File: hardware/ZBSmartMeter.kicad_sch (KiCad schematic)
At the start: 37 parts, among them J1 RJ12, J2 Conn_01x04, J3 Conn_01x02, J5 Screw_Terminal_01x02, J6 USB_C_Receptacle_USB2.0, SW1 SW_Push, SW2 SW_Push, U1 NCN5150DG, U2 TLV1117-33, U3 ESP32-C6-MINI-1/U

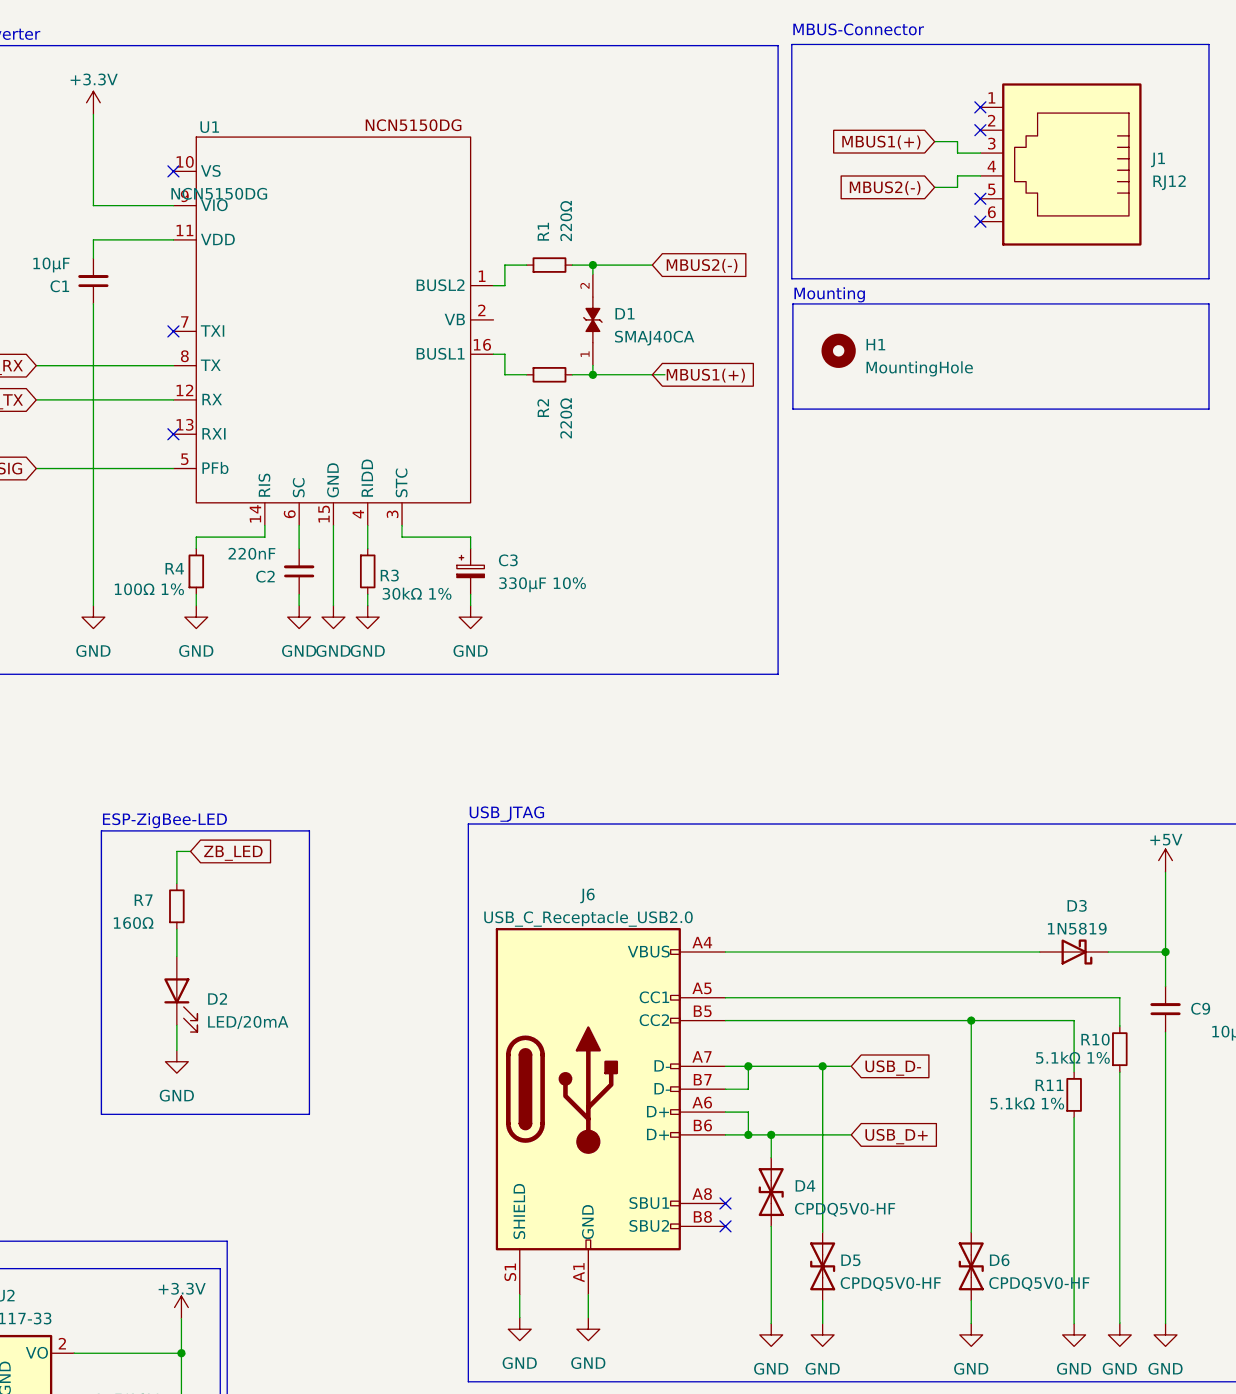
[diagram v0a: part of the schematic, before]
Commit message: fixed diode error, improved layout
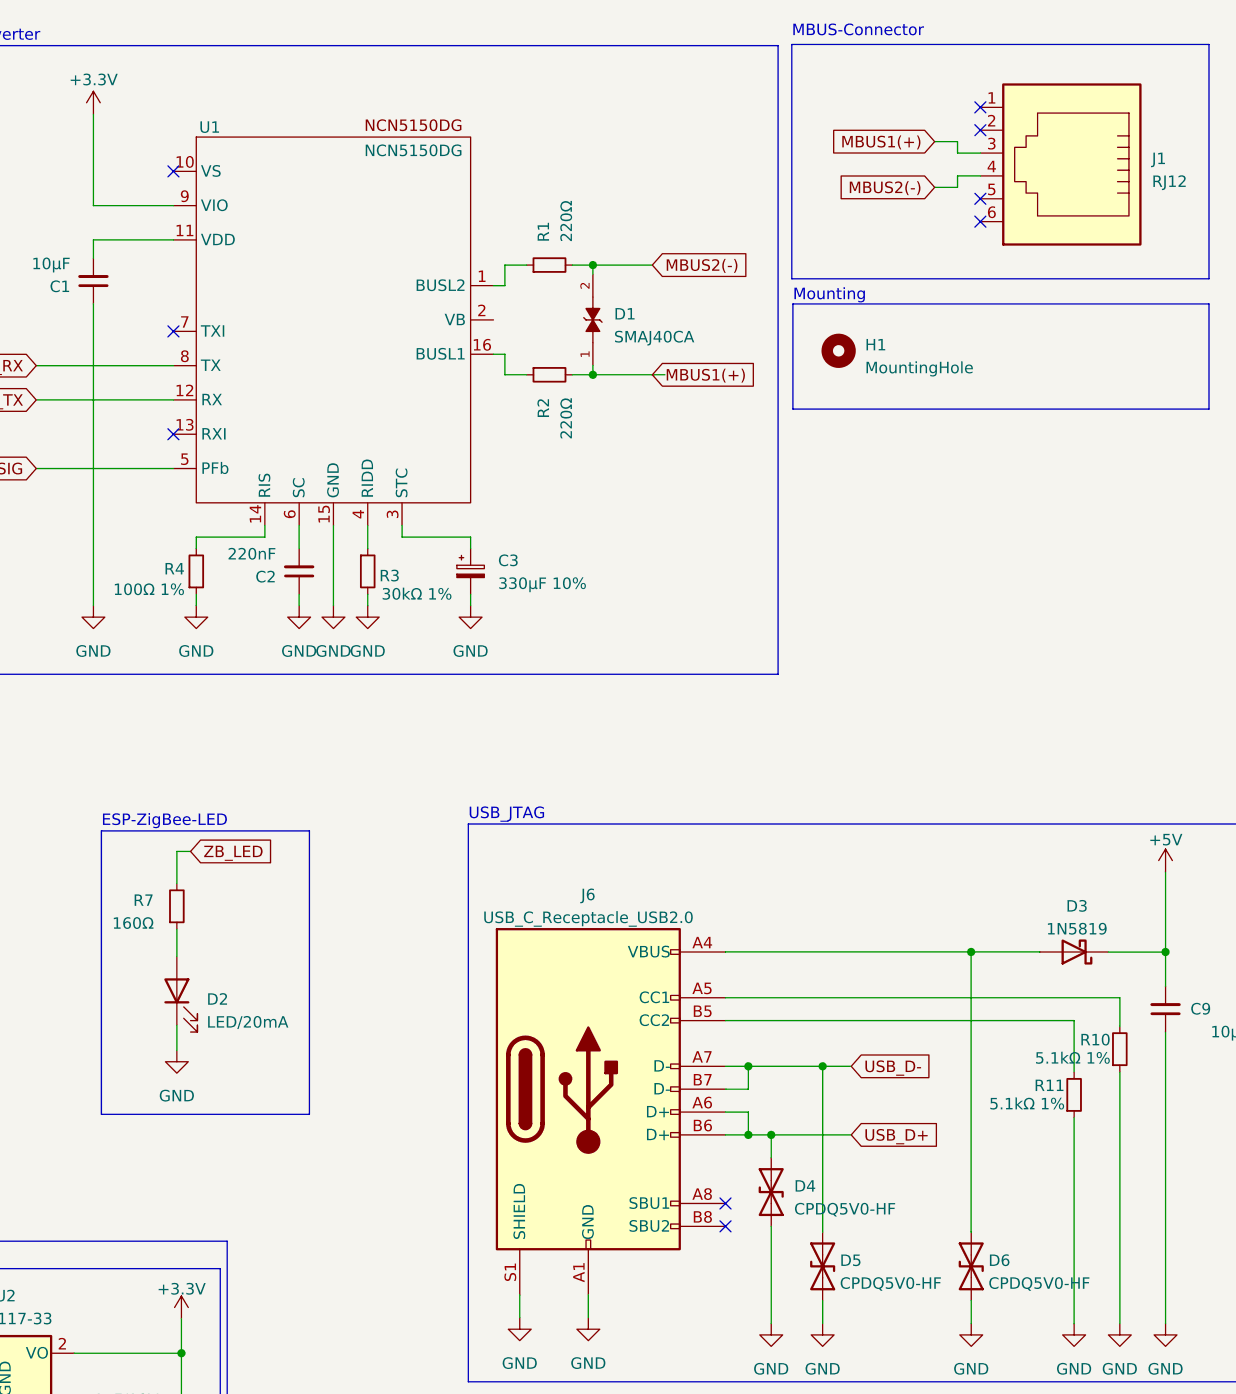
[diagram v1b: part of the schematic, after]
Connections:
- net at J6.B5 (CC2), R11.2: no longer D6.2 (A2)
- net at D3.2 (A), J6.A4 (VBUS), J6.A9 (VBUS)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: now also D6.2 (A2)
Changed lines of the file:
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@@
   (junction (at 217.805 128.397) (diameter 0) (color 0 0 0 0)
   )
-  (junction (at 242.57 123.317) (diameter 0) (color 0 0 0 0)
-  )
   (junction (at 264.16 115.697) (diameter 0) (color 0 0 0 0)
   )
@@
   )
   (junction (at 220.345 136.017) (diameter 0) (color 0 0 0 0)
+  )
+  (junction (at 242.5561 115.6919) (diameter 0) (color 0 0 0 0)
   )
   (junction (at 123.825 160.274) (diameter 0) (color 0 0 0 0)
@@
     (stroke (width 0) (type default))
   )
+  (wire (pts (xy 250.19 115.6919) (xy 250.19 115.697))
+    (stroke (width 0) (type default))
+  )
   (wire (pts (xy 145.034 43.688) (xy 145.034 77.216))
     (stroke (width 0) (type default))
@@
     (stroke (width 0) (type default))
   )
+  (wire (pts (xy 242.5561 115.6919) (xy 250.19 115.6919))
+    (stroke (width 0) (type default))
+  )
   (wire (pts (xy 77.47 130.556) (xy 77.47 132.334))
     (stroke (width 0) (type default))
@@
     (stroke (width 0) (type default))
   )
-  (wire (pts (xy 242.57 123.317) (xy 242.57 146.812))
-    (stroke (width 0) (type default))
-  )
   (wire (pts (xy 77.47 132.334) (xy 78.74 132.334))
     (stroke (width 0) (type default))
@@
     (stroke (width 0) (type default))
   )
+  (wire (pts (xy 215.265 115.6919) (xy 242.5561 115.6919))
+    (stroke (width 0) (type default))
+  )
   (wire (pts (xy 200.533 39.37) (xy 207.137 39.37))
     (stroke (width 0) (type default))
@@
     (stroke (width 0) (type default))
   )
+  (wire (pts (xy 242.5561 115.6919) (xy 242.5561 146.812))
+    (stroke (width 0) (type default))
+  )
   (wire (pts (xy 226.06 128.397) (xy 229.235 128.397))
     (stroke (width 0) (type default))
@@
     (stroke (width 0) (type default))
   )
-  (wire (pts (xy 215.265 123.317) (xy 242.57 123.317))
+  (wire (pts (xy 215.265 123.317) (xy 254 123.317))
     (stroke (width 0) (type default))
   )
@@
     (stroke (width 0) (type default))
   )
+  (wire (pts (xy 242.5561 146.812) (xy 242.57 146.812))
+    (stroke (width 0) (type default))
+  )
   (wire (pts (xy 145.034 32.766) (xy 153.924 32.766))
     (stroke (width 0) (type default))
@@
     (stroke (width 0) (type default))
   )
-  (wire (pts (xy 215.265 115.697) (xy 250.19 115.697))
-    (stroke (width 0) (type default))
-  )
   (wire (pts (xy 43.18 132.334) (xy 41.148 132.334))
     (stroke (width 0) (type default))
@@
     (stroke (width 0) (type default))
   )
-  (wire (pts (xy 242.57 123.317) (xy 254 123.317))
+  (wire (pts (xy 215.265 115.6919) (xy 215.265 115.697))
     (stroke (width 0) (type default))
   )
@@
       (effects (font (size 1.27 1.27)))
     )
-    (property "Value" "NCN5150DG" (at 159.004 31.496 0)
-      (effects (font (size 1.27 1.27)))
-    )
+    (property "Value" "NCN5150DG" (at 180.594 26.67 0)
+      (effects (font (size 1.27 1.27)))
+    )

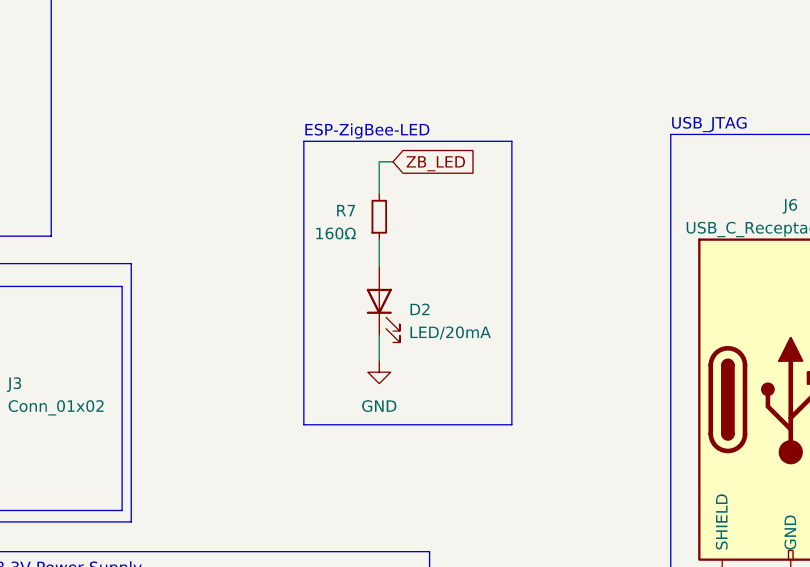
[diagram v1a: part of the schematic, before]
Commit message: LED to bright, change resistor value
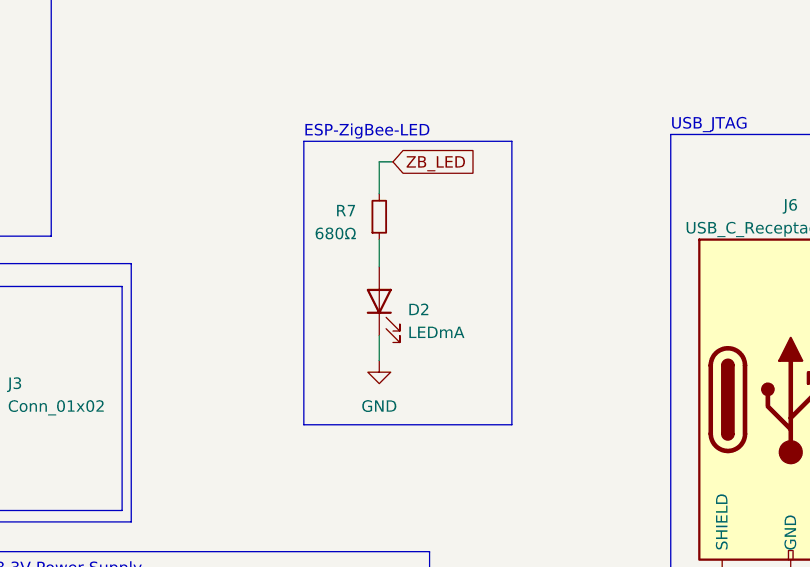
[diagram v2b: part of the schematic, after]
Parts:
- D2: value LED/20mA -> LEDmA
- R7: value 160Ω -> 680Ω
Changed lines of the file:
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@@
   (symbol (lib_id "Device:LED") (at 154.305 120.015 90) (unit 1)
     (in_bom yes) (on_board yes) (dnp no) (fields_autoplaced)
-    (property "Reference" "D2" (at 157.607 120.9675 90)
-      (effects (font (size 1.27 1.27)) (justify right))
-    )
-    (property "Value" "LED/20mA" (at 157.607 123.5075 90)
+    (property "Reference" "D2" (at 157.48 120.9675 90)
+      (effects (font (size 1.27 1.27)) (justify right))
+    )
+    (property "Value" "LEDmA" (at 157.48 123.5075 90)
       (effects (font (size 1.27 1.27)) (justify right))
     )
@@
       (effects (font (size 1.27 1.27)) (justify right))
     )
-    (property "Value" "160Ω" (at 151.765 112.522 0)
-      (effects (font (size 1.27 1.27)) (justify right))
-    )
+    (property "Value" "680Ω" (at 151.765 112.522 0)
+      (effects (font (size 1.27 1.27)) (justify right))
+    )

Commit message: dlms in progress
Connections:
- net UART1_PROG_RX renamed UART0_PROG_RX
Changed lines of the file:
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@@
     )
   )
-  (global_label "UART1_PROG_RX" (shape input) (at 33.782 132.334 180) (fields_autoplaced)
+  (global_label "UART0_PROG_RX" (shape input) (at 33.782 132.334 180) (fields_autoplaced)
     (effects (font (size 1.27 1.27)) (justify right))
     (property "Intersheetrefs" "${INTERSHEET_REFS}" (at 15.4548 132.334 0)
@@
     )
   )
-  (global_label "UART1_PROG_RX" (shape input) (at 93.726 46.736 0) (fields_autoplaced)
+  (global_label "UART0_PROG_RX" (shape input) (at 93.726 46.736 0) (fields_autoplaced)
     (effects (font (size 1.27 1.27)) (justify left))
     (property "Intersheetrefs" "${INTERSHEET_REFS}" (at 112.0532 46.736 0)
